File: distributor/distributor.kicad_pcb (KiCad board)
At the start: 2 copper layers, 91.5 x 52 mm, 14 parts, among them J1 Cerebellum, J10 CAN FD, J2 Cerebrum, J3 XT60PW-M, J4 CAN FD, J5 LegL, J6 ArmL, J7 LegR, J8 ArmR, J9 XT60PW-M

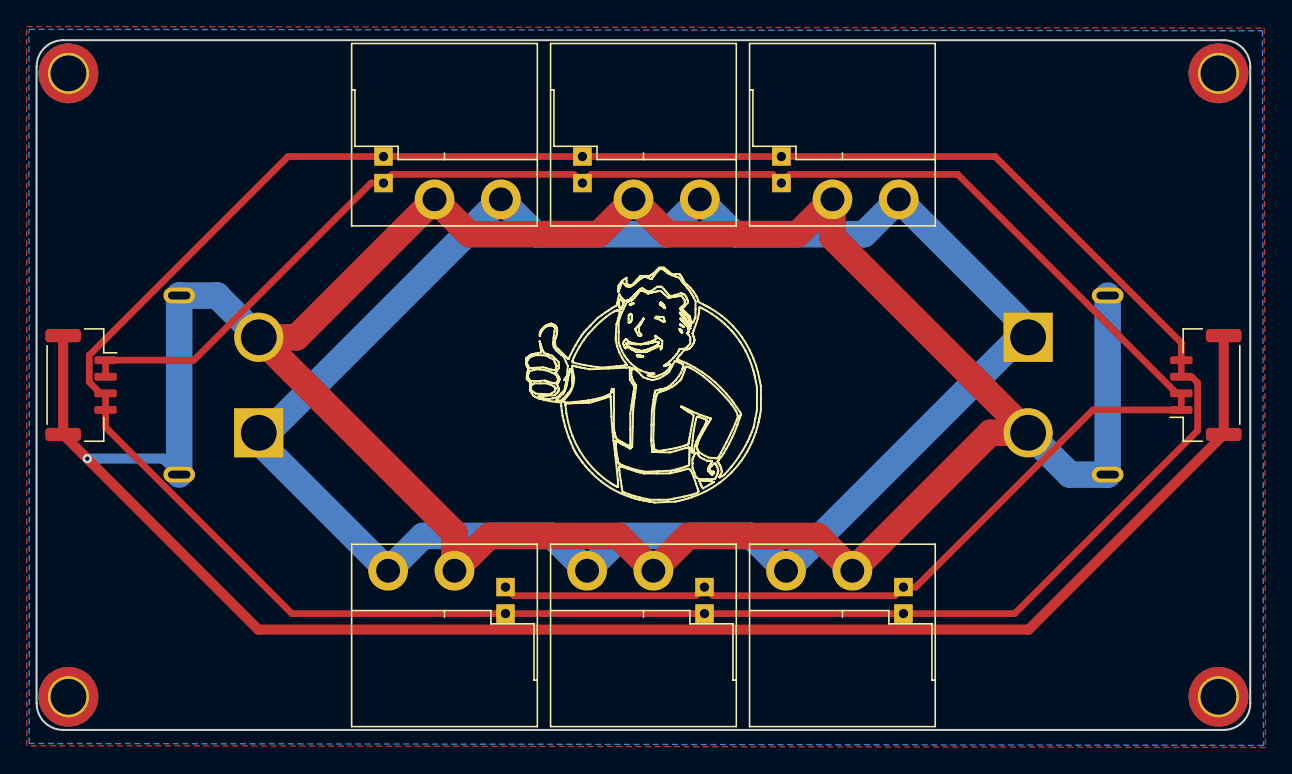
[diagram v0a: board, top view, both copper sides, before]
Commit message: [Modify] Remove XT30(2+2), replaced by XT30 + GH 2pins
XT30(2+2) is not as robust as expected, so I replace all ports by XT30 and JST GH 1.25mm 2pin.
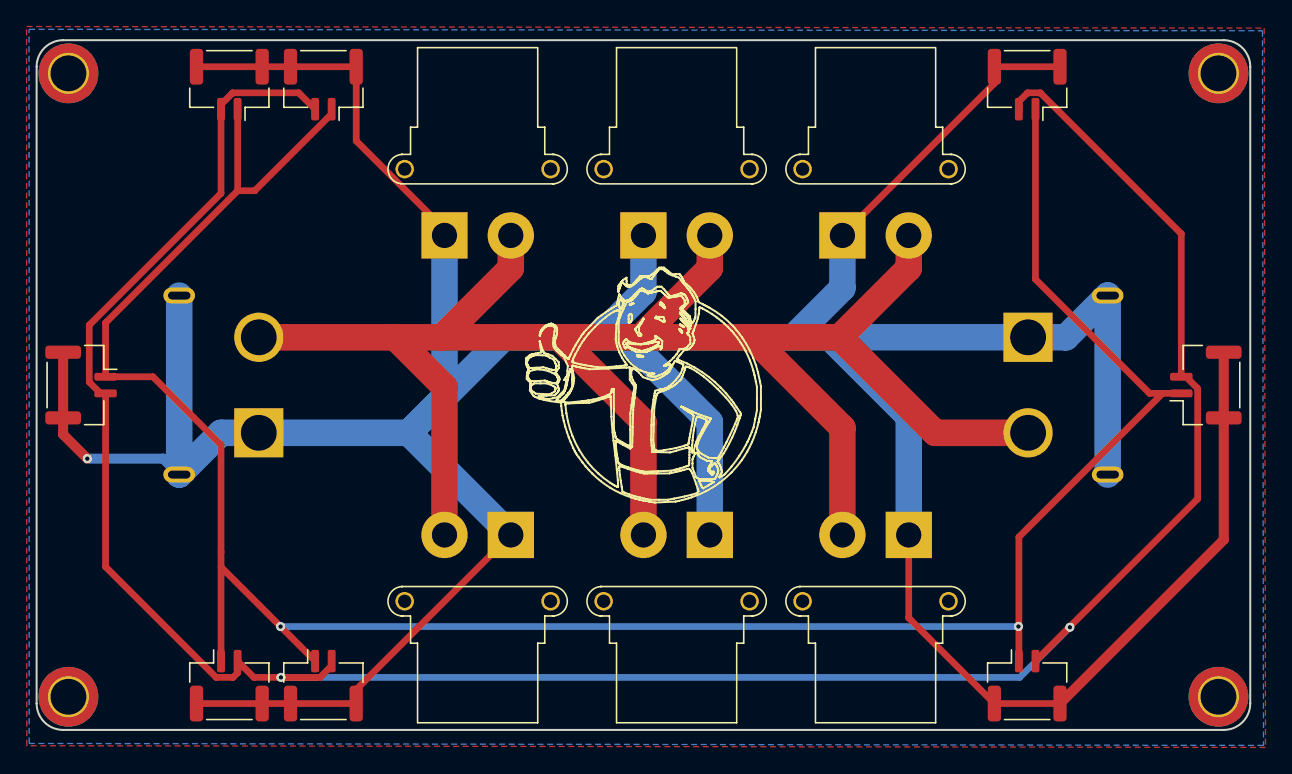
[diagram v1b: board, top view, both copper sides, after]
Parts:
- added J11: CAN FD, Connector_JST:JST_GH_SM02B-GHS-TB_1x02-1MP_P1.25mm_Horizontal, F.Cu at (178.9, 122.7)
- added J12: CAN FD, Connector_JST:JST_GH_SM02B-GHS-TB_1x02-1MP_P1.25mm_Horizontal, F.Cu at (125.9, 122.7)
- added J13: CAN FD, Connector_JST:JST_GH_SM02B-GHS-TB_1x02-1MP_P1.25mm_Horizontal, F.Cu at (118.8, 77.3)
- added J14: CAN FD, Connector_JST:JST_GH_SM02B-GHS-TB_1x02-1MP_P1.25mm_Horizontal, F.Cu at (178.9, 77.3)
- added J15: CAN FD, Connector_JST:JST_GH_SM02B-GHS-TB_1x02-1MP_P1.25mm_Horizontal, F.Cu at (118.8, 122.7)
- added J16: CAN FD, Connector_JST:JST_GH_SM02B-GHS-TB_1x02-1MP_P1.25mm_Horizontal, F.Cu at (125.9, 77.3)
- J1, J2, J5, J6, J7, J8: footprint Rolling_Custom:XT30PW(2+2) -> Connector_AMASS:AMASS_XT30PW-F_1x02_P2.50mm_Horizontal
- J10, J4: footprint Connector_JST:JST_GH_SM04B-GHS-TB_1x04-1MP_P1.25mm_Horizontal -> Connector_JST:JST_GH_SM02B-GHS-TB_1x02-1MP_P1.25mm_Horizontal
- J3, J9: value XT60PW-M -> PowerIO
- moved J1 5.68 mm to (155.0, 111.3), turned to 180 degrees
- moved J6 5.68 mm to (170.0, 111.3), turned to 180 degrees
- moved J7 5.68 mm to (140.0, 111.3), turned to 180 degrees
- moved J2 2.72 mm to (150.0, 88.7), turned to 0 degrees
- moved J5 2.72 mm to (135.0, 88.7), turned to 0 degrees
- moved J8 2.72 mm to (165.0, 88.7), turned to 0 degrees
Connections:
- J1 pad 1: +24V -> GNDA
- J1 pad 2: GNDA -> +24V
- J10 pad 2: CANFD_H -> CANFD_L
- J2 pad 1: +24V -> GNDA
- J2 pad 2: GNDA -> +24V
- J3 pad 1: +24V -> GNDA
- J3 pad 2: GNDA -> +24V
- J4 pad 2: CANFD_H -> CANFD_L
- J5 pad 1: +24V -> GNDA
- J5 pad 2: GNDA -> +24V
- J6 pad 1: +24V -> GNDA
- J6 pad 2: GNDA -> +24V
- J7 pad 1: +24V -> GNDA
- J7 pad 2: GNDA -> +24V
- J8 pad 1: +24V -> GNDA
- J8 pad 2: GNDA -> +24V
- J9 pad 1: +24V -> GNDA
- J9 pad 2: GNDA -> +24V
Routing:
- net CANFD_H: track 154.9 -> 178.8 mm, vias 0 -> 2
- net GNDA: track 314.9 -> 330.9 mm
- net CANFD_L: track 202.0 -> 187.0 mm, vias 0 -> 2
- net +24V: track 148.7 -> 142.2 mm
- added copper zone on F.Cu, net +24V
- added copper zone on B.Cu, net GNDA
- removed copper zone on B.Cu, net +24V
- removed copper zone on F.Cu, net GNDA

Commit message: [New] Add 24V to 5V converter to distributor
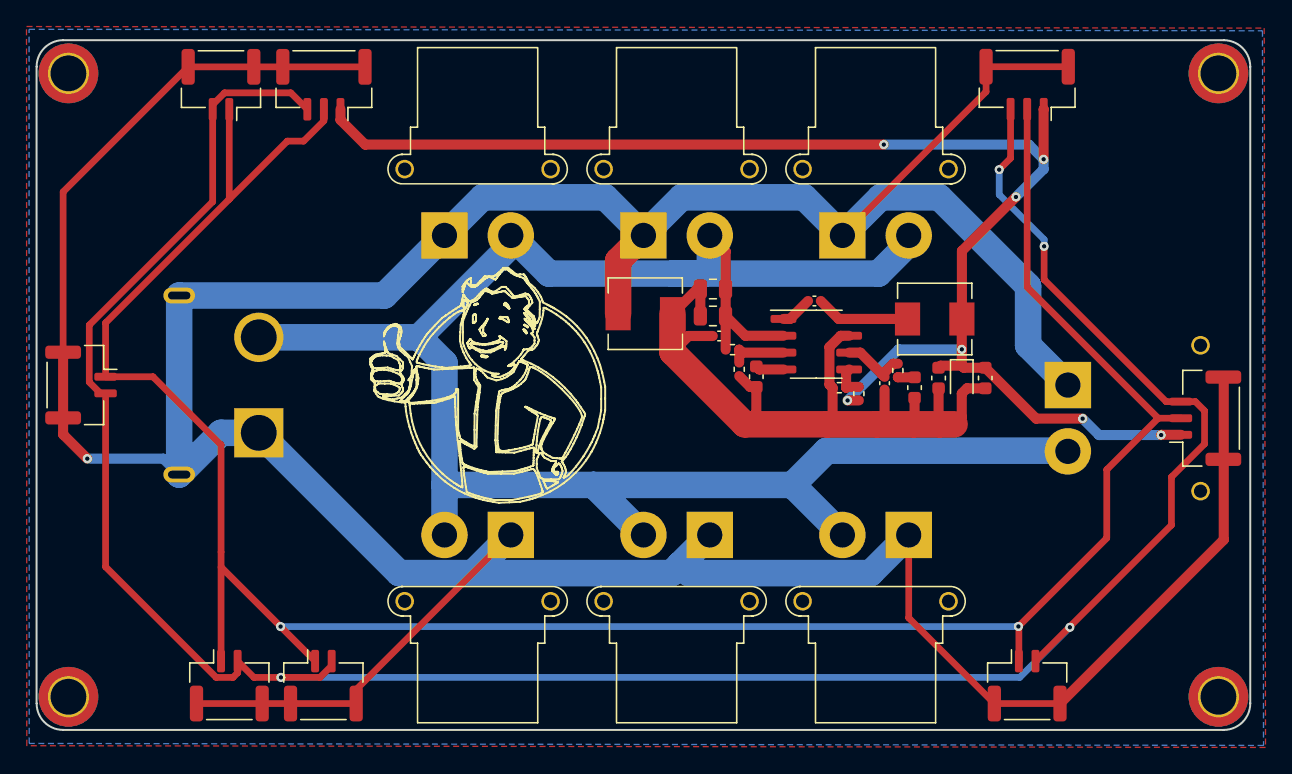
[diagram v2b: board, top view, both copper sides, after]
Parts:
- added C1: 10pf/50V/0402, Capacitor_SMD:C_0402_1005Metric, F.Cu at (168.2, 99.9)
- added C2: 1.5nf/50V/0603, Capacitor_SMD:C_0603_1608Metric, F.Cu at (170.4, 100.2)
- added C3: 4.7uF/50V/0805, Capacitor_SMD:C_0805_2012Metric, F.Cu at (155.2, 92.8)
- added C4: 4.7uF/50V/0805, Capacitor_SMD:C_0805_2012Metric, F.Cu at (155.2, 94.8)
- added C5: 10uf/50V/0402, Capacitor_SMD:C_0402_1005Metric, F.Cu at (155.7, 96.3)
- added C6: 8.2nf/50V/0603, Capacitor_SMD:C_0603_1608Metric, F.Cu at (158.5, 99.4)
- added C7: 100nF/10V/0402, Capacitor_SMD:C_0402_1005Metric, F.Cu at (162.9, 93.7)
- added C8: 47uf/50V/0603, Capacitor_SMD:C_0603_1608Metric, F.Cu at (172.2, 99.5)
- added C9: 47uf/50V/0603, Capacitor_SMD:C_0603_1608Metric, F.Cu at (175.8, 99.5)
- added D1: BZT52C5V1S, Diode_SMD:D_SOD-323, F.Cu at (174.0, 99.6)
- added L1: 15uh/SLO0530H150MTT, Inductor_SMD:L_Sunlord_MWSA0518_5.4x5.2mm, F.Cu at (172.0, 95.0)
- added L2: 15uh/SLO0530H150MTT, Inductor_SMD:L_Sunlord_MWSA0518_5.4x5.2mm, F.Cu at (150.1, 94.6)
- added R1: 64.9k/0402, Resistor_SMD:R_0402_1005Metric, F.Cu at (169.2, 98.9)
- added R2: 169k/0402, Resistor_SMD:R_0402_1005Metric, F.Cu at (156.7, 97.3)
- added R3: 20.5k/0402, Resistor_SMD:R_0402_1005Metric, F.Cu at (157.2, 98.8)
- added R4: 10.2k/0402, Resistor_SMD:R_0402_1005Metric, F.Cu at (166.2, 100.7)
- added R5: 1.96k/0402, Resistor_SMD:R_0402_1005Metric, F.Cu at (164.8, 100.2)
- added U1: TPS54231, Package_SO:SOIC-8_3.9x4.9mm_P1.27mm, F.Cu at (163.0, 96.9)
- J14: value CAN FD -> ArmR; footprint Connector_JST:JST_GH_SM02B-GHS-TB_1x02-1MP_P1.25mm_Horizontal -> Connector_JST:JST_GH_SM03B-GHS-TB_1x03-1MP_P1.25mm_Horizontal
- J16: value CAN FD -> ArmL; footprint Connector_JST:JST_GH_SM02B-GHS-TB_1x02-1MP_P1.25mm_Horizontal -> Connector_JST:JST_GH_SM03B-GHS-TB_1x03-1MP_P1.25mm_Horizontal
- J3: footprint Rolling_Custom:AMASS_XT60PW-M -> Connector_AMASS:AMASS_XT30PW-M_1x02_P2.50mm_Horizontal
- J4: value CAN FD -> Back; footprint Connector_JST:JST_GH_SM02B-GHS-TB_1x02-1MP_P1.25mm_Horizontal -> Connector_JST:JST_GH_SM03B-GHS-TB_1x03-1MP_P1.25mm_Horizontal
- moved J3 3.00 mm to (182.0, 100.0)
- moved J4 2.50 mm to (192.4, 102.5)
- moved J13 0.63 mm to (118.2, 77.4)
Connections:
- J14 pad 1: CANFD_H -> +5V
- J14 pad 2: CANFD_L -> CANFD_H
- J16 pad 1: CANFD_H -> +5V
- J16 pad 2: CANFD_L -> CANFD_H
- J4 pad 1: CANFD_H -> +5V
- J4 pad 2: CANFD_L -> CANFD_H
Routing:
- net +5V: track 0.00 -> 108.5 mm, vias 0 -> 7
- net GND: track 0.00 -> 59.7 mm
- net +24V: track 142.2 -> 149.3 mm
- net Net-(C7-Pad1): track 0.00 -> 7.10 mm
- net 5V_CMP: track 0.00 -> 4.94 mm
- net Net-(R2-Pad2): track 0.00 -> 4.40 mm
- net 5V_FB: track 0.00 -> 2.45 mm
- net Net-(C7-Pad2): track 0.00 -> 2.42 mm
- net Net-(C6-Pad1): track 0.00 -> 2.14 mm
- net Net-(C2-Pad1): track 0.00 -> 1.26 mm
- net CANFD_L: track 187.0 -> 186.2 mm, vias 2 -> 4

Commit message: [New] Release all board 3D models
* All files are in folder "steps".
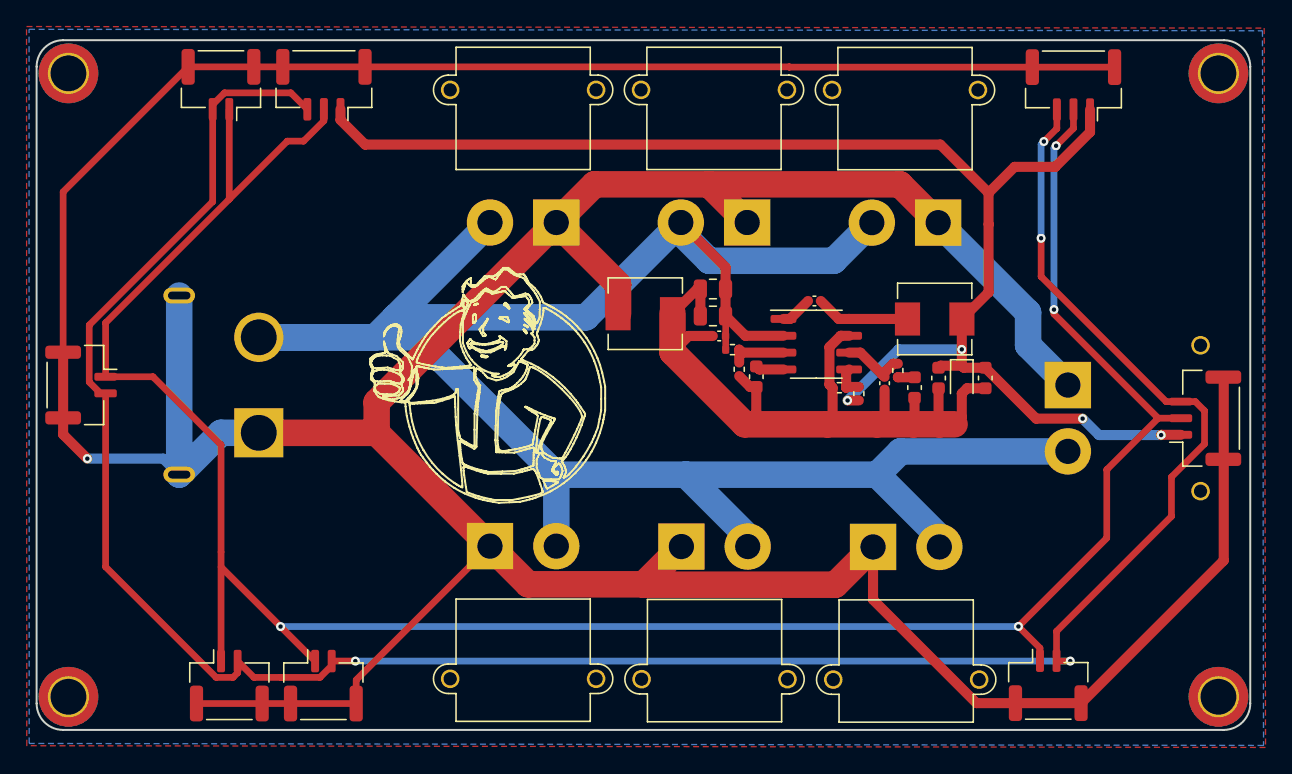
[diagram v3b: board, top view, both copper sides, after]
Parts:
- J1, J2, J5, J6, J7, J8: footprint Connector_AMASS:AMASS_XT30PW-F_1x02_P2.50mm_Horizontal -> Connector_AMASS:AMASS_XT30PW-M_1x02_P2.50mm_Horizontal
- moved J2 22.2 mm to (172.2, 87.8)
- moved J5 8.49 mm to (143.4, 87.7)
- moved J8 7.25 mm to (157.8, 87.7)
- moved J14 3.49 mm to (182.4, 77.4)
- moved J6 2.84 mm to (167.3, 112.2)
- moved J1 2.31 mm to (152.9, 112.2)
- moved J7 1.78 mm to (138.4, 112.1)
- moved J11 1.59 mm to (180.5, 122.6)
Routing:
- net GNDA: track 331.0 -> 350.3 mm
- net +24V: track 149.3 -> 164.8 mm
- net CANFD_L: track 186.2 -> 179.9 mm
- net CANFD_H: track 179.1 -> 179.4 mm, vias 2 -> 4
- net +5V: track 108.5 -> 108.6 mm, vias 7 -> 4
- added copper zone on B.Cu, net +24V
- added copper zone on F.Cu, net GNDA
- removed copper zone on F.Cu, net +24V
- removed copper zone on B.Cu, net GNDA

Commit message: [Fix] Correct mounting hole positions
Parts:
- J13, J15: footprint Connector_JST:JST_GH_SM02B-GHS-TB_1x02-1MP_P1.25mm_Horizontal -> Connector_JST:JST_GH_SM04B-GHS-TB_1x04-1MP_P1.25mm_Horizontal
- moved J11 77.0 mm to (118.2, 77.4), turned to 180 degrees
- moved J14 72.4 mm to (125.9, 122.6), turned to 0 degrees
- moved J13 63.7 mm to (181.8, 77.4)
- moved J15 63.0 mm to (181.8, 122.6)
- moved J12 7.69 mm to (118.2, 122.6)
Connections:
- J13 pad 2: CANFD_L -> CANFD_H
- J15 pad 2: CANFD_L -> CANFD_H
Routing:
- net +5V: track 108.6 -> 149.3 mm, vias 4 -> 6
- net GNDA: track 350.3 -> 381.9 mm
- net CANFD_H: track 179.4 -> 195.1 mm
- net CANFD_L: track 179.9 -> 186.3 mm

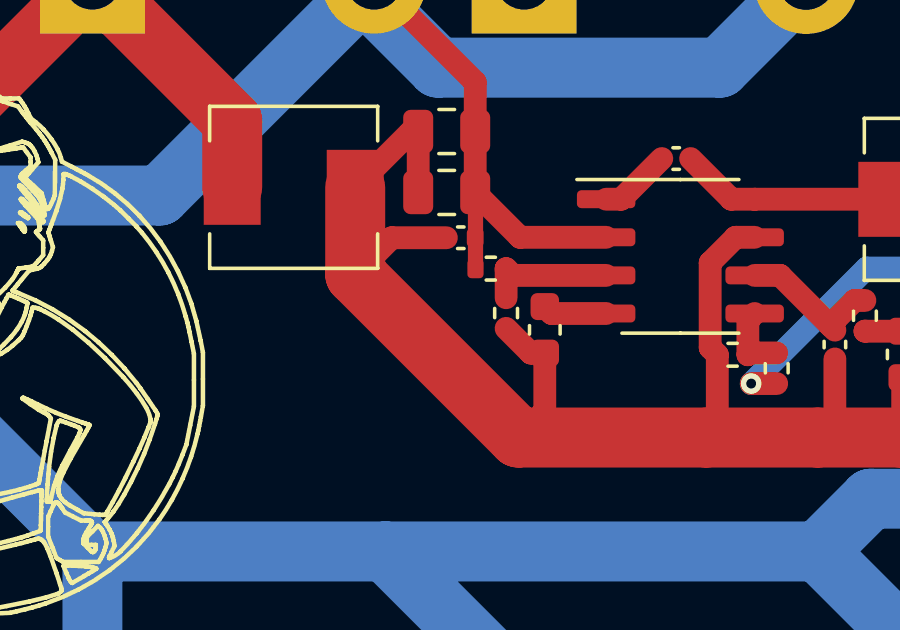
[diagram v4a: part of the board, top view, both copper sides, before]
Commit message: [Fix] Correct capacities in 24Vto5V converter
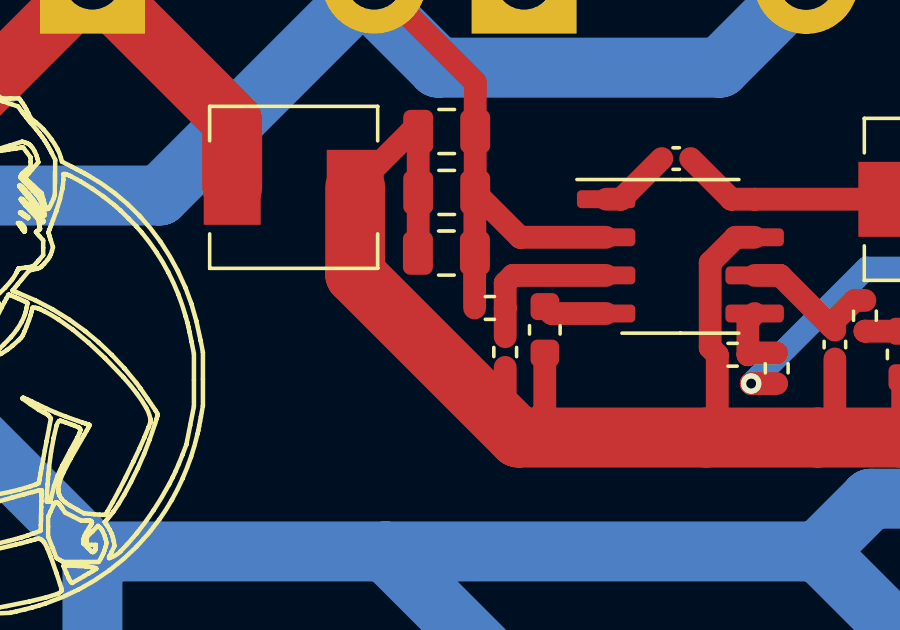
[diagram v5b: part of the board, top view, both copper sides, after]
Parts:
- C5: value 10uf/50V/0402 -> 10uf/50V/0805; footprint Capacitor_SMD:C_0402_1005Metric -> Capacitor_SMD:C_0805_2012Metric
- moved R2 1.31 mm to (156.7, 98.6)
- moved R3 1.30 mm to (157.2, 100.1)
- moved C5 0.70 mm to (155.2, 96.8)
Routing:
- net +24V: track 164.8 -> 166.2 mm
- net Net-(R2-Pad2): track 4.40 -> 5.26 mm
- net GND: track 59.7 -> 59.1 mm
